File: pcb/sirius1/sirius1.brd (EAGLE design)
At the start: 154 x 123 mm, 18 parts

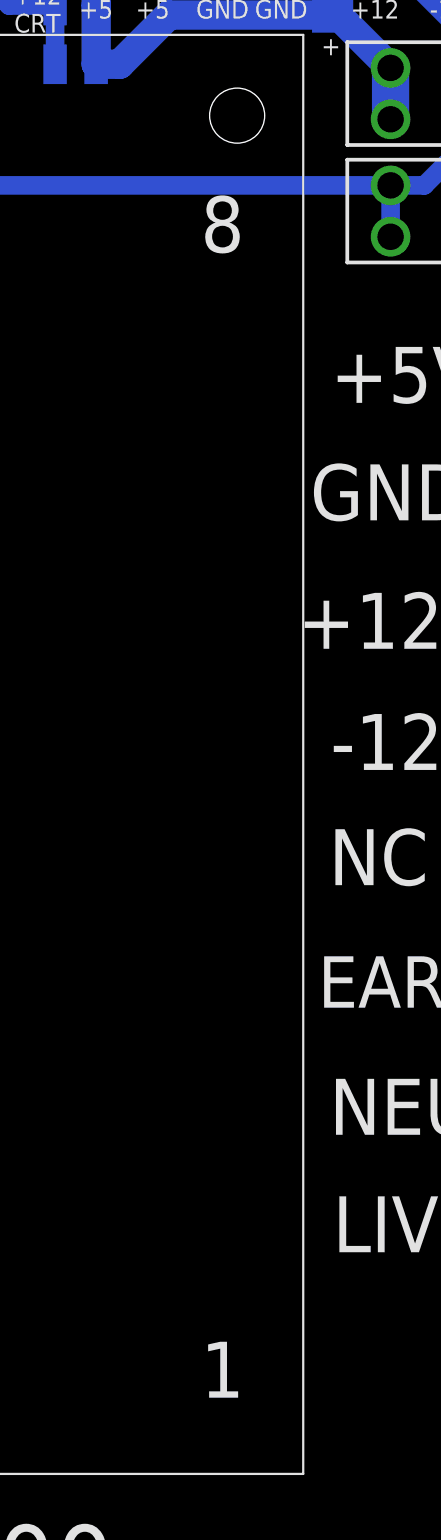
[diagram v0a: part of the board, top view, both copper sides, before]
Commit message: adjusted silkscreen
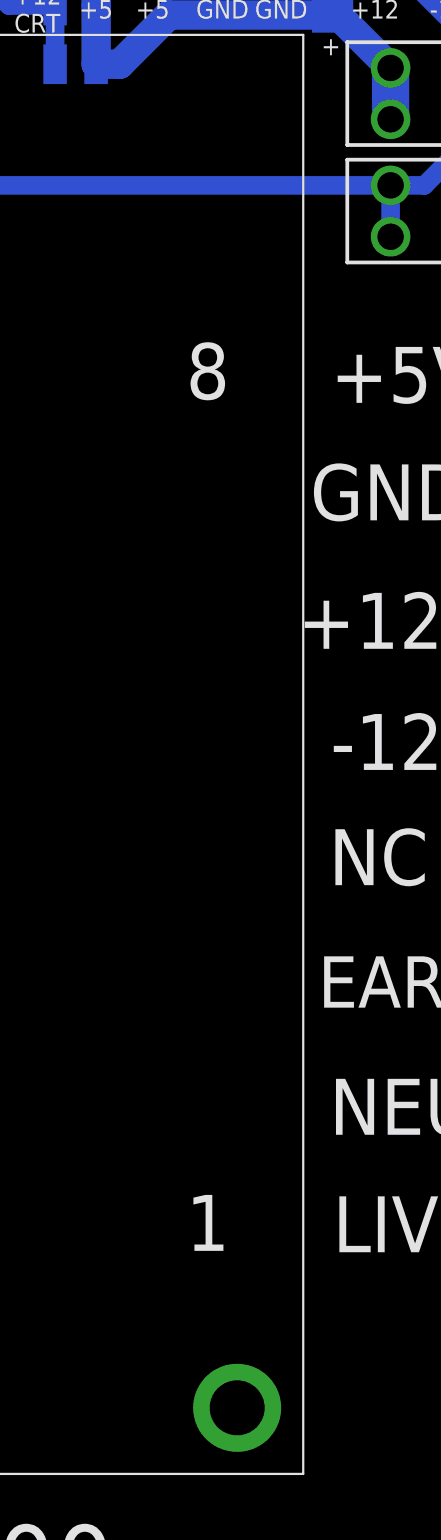
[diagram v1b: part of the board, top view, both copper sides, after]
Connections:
- net GND: now also U$7.GND1
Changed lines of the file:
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@@
 <layer number="14" name="Route14" color="22" fill="1" visible="no" active="no"/>
 <layer number="15" name="Route15" color="23" fill="1" visible="no" active="no"/>
-<layer number="16" name="Bottom" color="1" fill="1" visible="no" active="yes"/>
+<layer number="16" name="Bottom" color="1" fill="1" visible="yes" active="yes"/>
 <layer number="17" name="Pads" color="2" fill="1" visible="yes" active="yes"/>
 <layer number="18" name="Vias" color="2" fill="1" visible="yes" active="yes"/>
@@
 <layer number="20" name="Dimension" color="24" fill="1" visible="yes" active="yes"/>
 <layer number="21" name="tPlace" color="7" fill="1" visible="yes" active="yes"/>
-<layer number="22" name="bPlace" color="7" fill="1" visible="no" active="yes"/>
+<layer number="22" name="bPlace" color="7" fill="1" visible="yes" active="yes"/>
 <layer number="23" name="tOrigins" color="15" fill="1" visible="yes" active="yes"/>
-<layer number="24" name="bOrigins" color="15" fill="1" visible="no" active="yes"/>
+<layer number="24" name="bOrigins" color="15" fill="1" visible="yes" active="yes"/>
 <layer number="25" name="tNames" color="7" fill="1" visible="yes" active="yes"/>
-<layer number="26" name="bNames" color="7" fill="1" visible="no" active="yes"/>
-<layer number="27" name="tValues" color="7" fill="1" visible="no" active="yes"/>
-<layer number="28" name="bValues" color="7" fill="1" visible="no" active="yes"/>
+<layer number="26" name="bNames" color="7" fill="1" visible="yes" active="yes"/>
+<layer number="27" name="tValues" color="7" fill="1" visible="yes" active="yes"/>
+<layer number="28" name="bValues" color="7" fill="1" visible="yes" active="yes"/>
 <layer number="29" name="tStop" color="7" fill="3" visible="no" active="yes"/>
 <layer number="30" name="bStop" color="7" fill="6" visible="no" active="yes"/>
@@
 <layer number="38" name="bTest" color="7" fill="1" visible="no" active="yes"/>
 <layer number="39" name="tKeepout" color="4" fill="11" visible="yes" active="yes"/>
-<layer number="40" name="bKeepout" color="1" fill="11" visible="no" active="yes"/>
+<layer number="40" name="bKeepout" color="1" fill="11" visible="yes" active="yes"/>
 <layer number="41" name="tRestrict" color="4" fill="10" visible="yes" active="yes"/>
-<layer number="42" name="bRestrict" color="1" fill="10" visible="no" active="yes"/>
+<layer number="42" name="bRestrict" color="1" fill="10" visible="yes" active="yes"/>
 <layer number="43" name="vRestrict" color="2" fill="10" visible="no" active="yes"/>
 <layer number="44" name="Drills" color="7" fill="1" visible="yes" active="yes"/>
@@
 <layer number="50" name="dxf" color="7" fill="1" visible="no" active="no"/>
 <layer number="51" name="tDocu" color="7" fill="1" visible="yes" active="yes"/>
-<layer number="52" name="bDocu" color="7" fill="1" visible="no" active="yes"/>
+<layer number="52" name="bDocu" color="7" fill="1" visible="yes" active="yes"/>
 <layer number="53" name="tGND_GNDA" color="7" fill="1" visible="no" active="no"/>
 <layer number="54" name="bGND_GNDA" color="7" fill="1" visible="no" active="no"/>
@@
 <vertex x="134.5" y="38"/>
 </polygon>
+<contactref element="U$7" pad="GND1"/>
 </signal>
 <signal name="+12V">

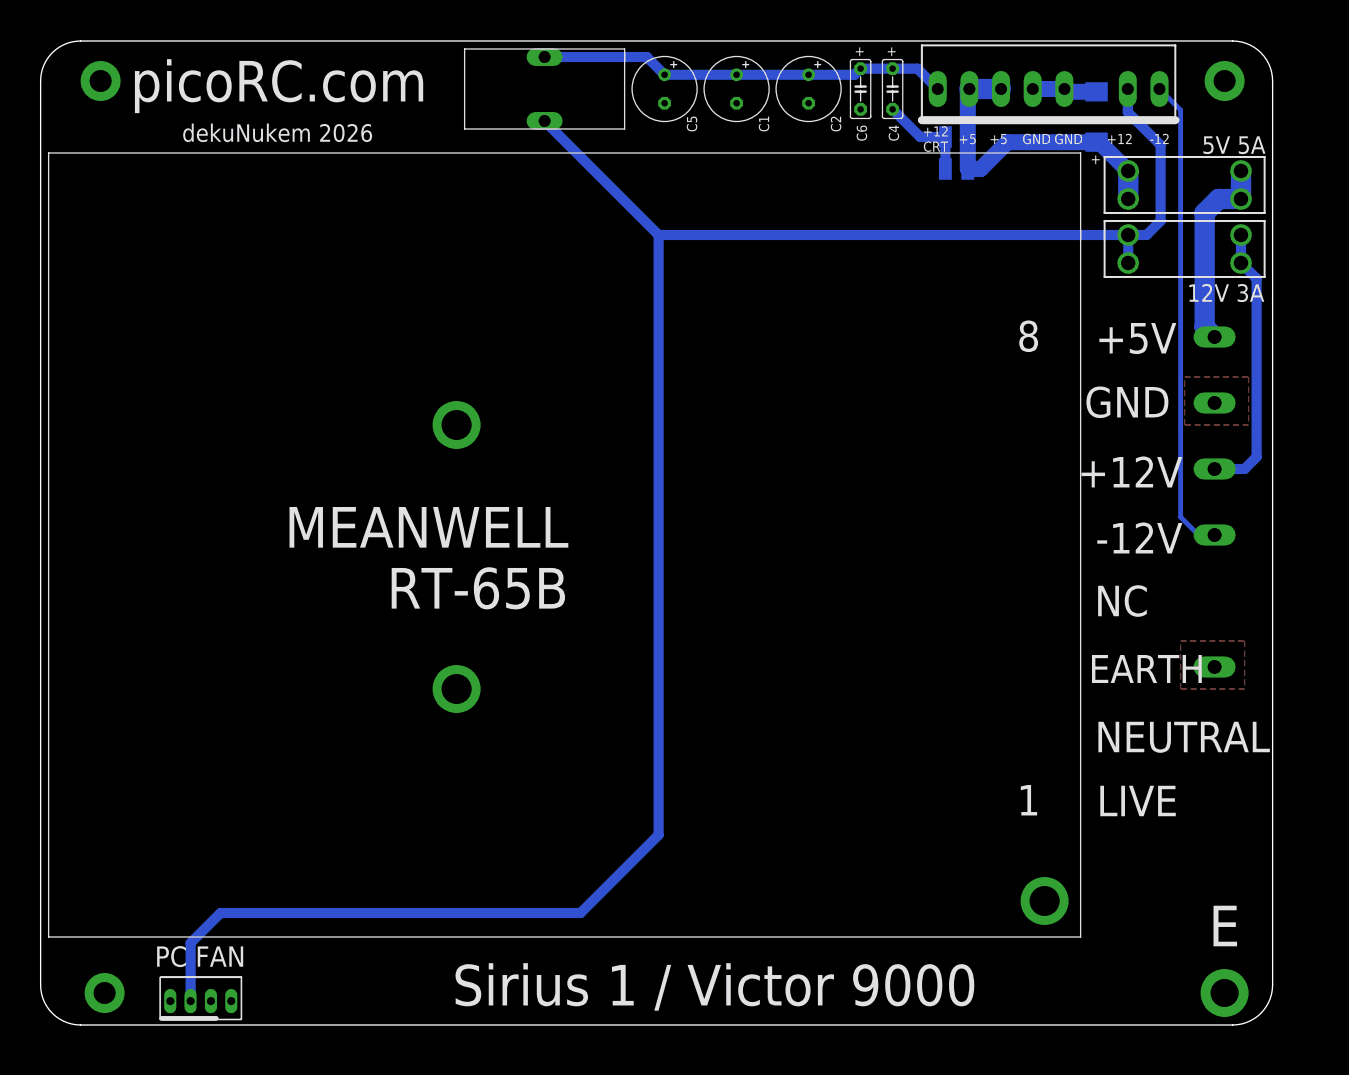
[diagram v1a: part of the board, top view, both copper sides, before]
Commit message: m3 holes, moved PSU down slighly, thicker 12V trace
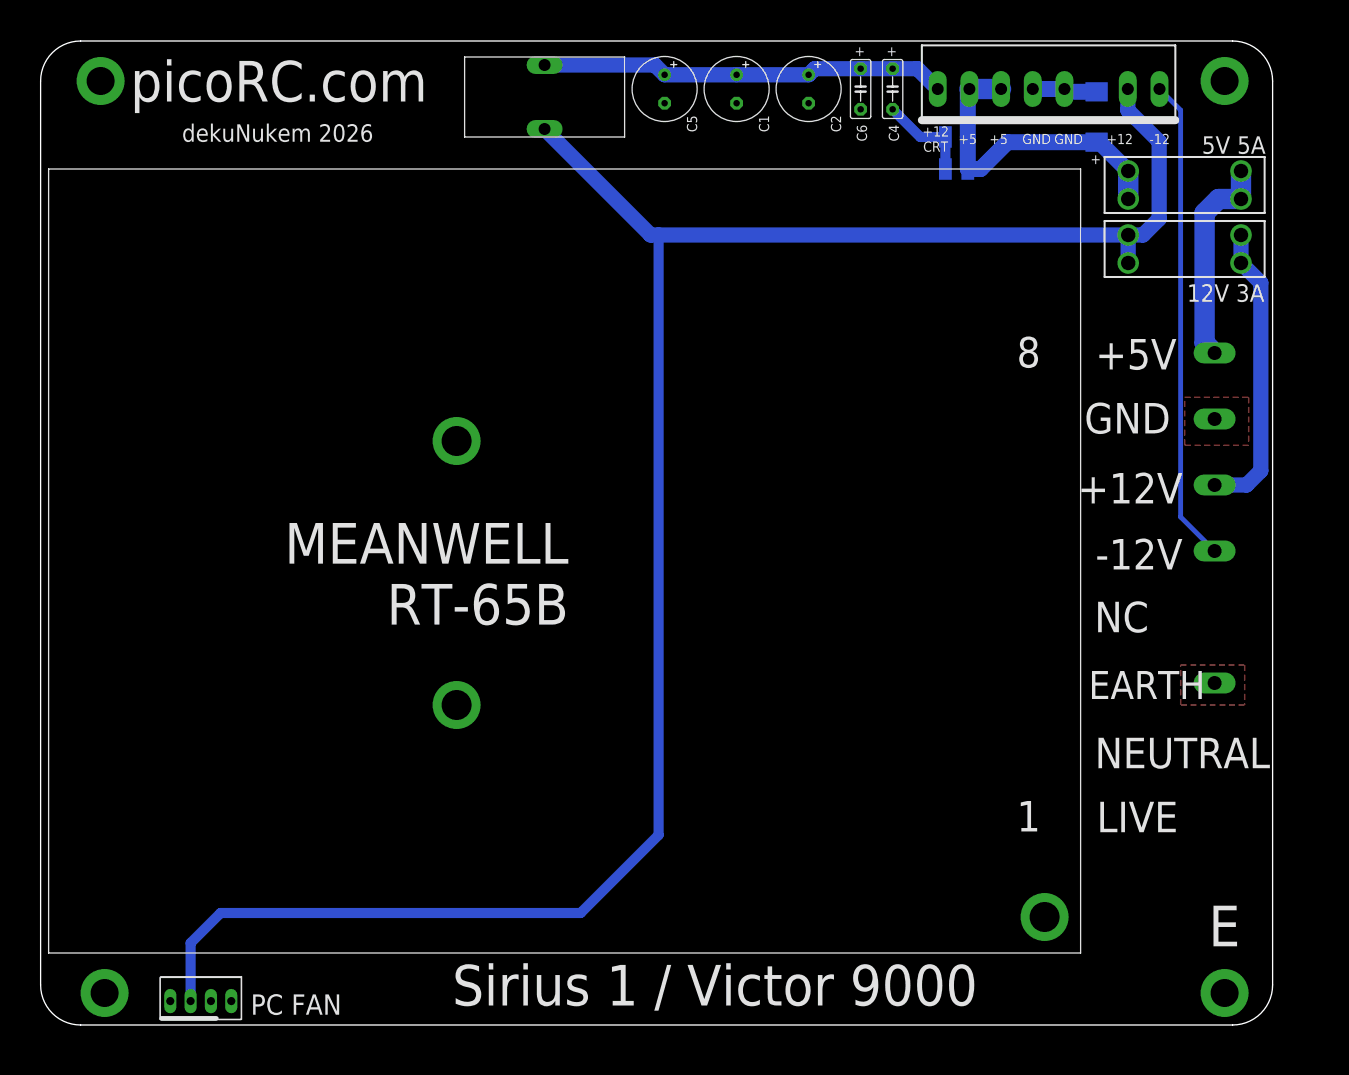
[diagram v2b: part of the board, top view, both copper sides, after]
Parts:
- U$2, U$4, U$5: value M3_HOLE_PLATEDM2,5 -> M3_HOLE_PLATEDM3; device os1:M2.5_HOLE_PLATED -> os1:M3_HOLE_PLATED
- moved U$7 2.00 mm to (122.0, 103.0)
- moved U$10 1.00 mm to (55.0, 112.0)
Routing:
- net N$4: track 34.4 -> 37.0 mm
- net N$2: track 24.8 -> 26.8 mm
- net -12V: track 59.8 -> 60.6 mm
- net +12V: track 251.7 -> 250.9 mm
